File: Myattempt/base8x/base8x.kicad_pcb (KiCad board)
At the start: 4 copper layers, 350 x 110 mm, 58 parts, among them J1 Conn_02x05_Odd_Even, J10 Conn_02x14_Counter_Clockwise, J11 Conn_02x14_Counter_Clockwise, J12 Conn_02x14_Counter_Clockwise, J13 Conn_02x14_Counter_Clockwise, J14 Conn_02x14_Counter_Clockwise, J15 Conn_02x14_Counter_Clockwise, J16 Conn_01x14, J2 GS3, J3 Conn_02x14_Counter_Clockwise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

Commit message: My work implementing resistor for sensor
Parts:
- removed J10, J11, J12, J13, J14, J15: Conn_02x14_Counter_Clockwise, Connector_PinSocket_2.54mm:PinSocket_2x14_P2.54mm_Vertical
- removed J16: Conn_01x14, Connector_PinSocket_2.54mm:PinSocket_1x14_P2.54mm_Vertical
- added Raspberry_header1: Conn_02x20_Odd_Even, Connector_PinSocket_2.54mm:PinSocket_2x20_P2.54mm_Vertical, F.Cu at (-51.4, -26.7)
- added Resistor1: 4.7k, Resistor_THT:R_Axial_DIN0617_L17.0mm_D6.0mm_P20.32mm_Horizontal, F.Cu at (-94.0, -10.8)
- added Temp_sensor1: Conn_01x03_Female, Connector_PinSocket_2.54mm:PinSocket_1x03_P2.54mm_Vertical, F.Cu at (-110.5, -13.3)
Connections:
- J3 pad 10: Net-(J3-Pad10) -> SCL
- J3 pad 14: Net-(J3-Pad14) -> MISO
- J3 pad 16: Net-(J3-Pad16) -> MOSI
- J3 pad 8: Net-(J3-Pad8) -> SDA
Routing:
- net +3V3: track 37.4 -> 189.2 mm
- net GND: track 1.57 -> 77.4 mm
- net CLK0: track 0.00 -> 72.7 mm
- net +5V: track 2.43 -> 55.2 mm
- net SCL: track 139.5 -> 180.1 mm
- net SDA: track 130.8 -> 171.5 mm
- net MOSI: track 93.0 -> 129.0 mm
- net MISO: track 90.2 -> 124.2 mm

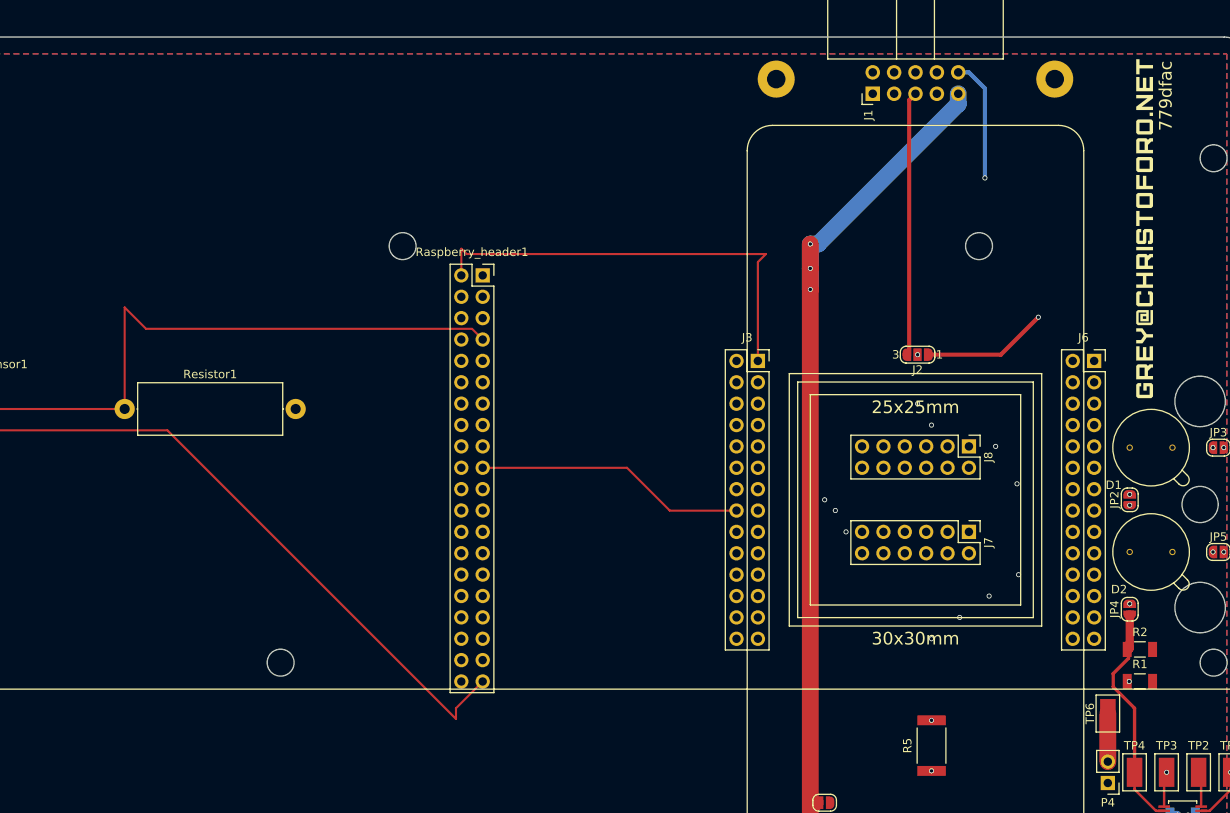
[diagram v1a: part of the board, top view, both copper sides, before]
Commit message: adding ssr and sensor
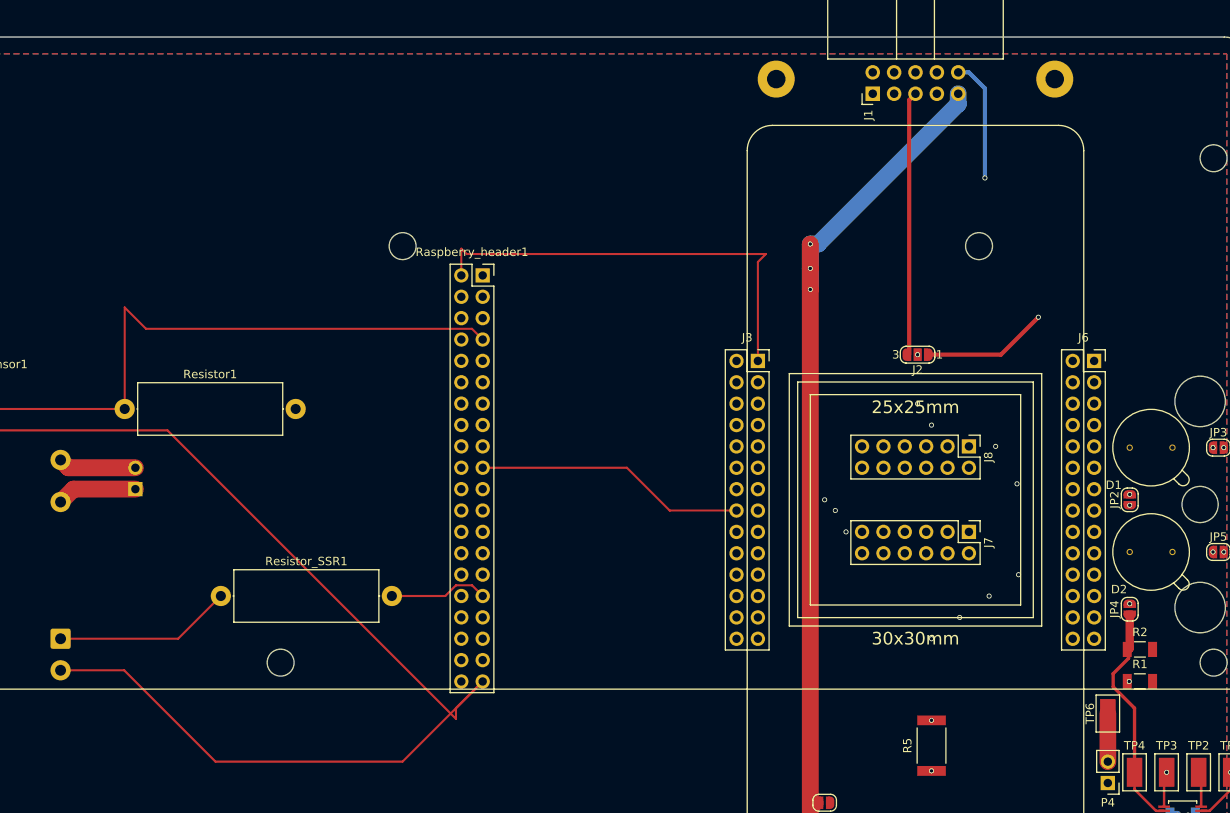
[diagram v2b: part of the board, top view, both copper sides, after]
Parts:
- removed L1: GREY@CHRISTOFORO.NET, myParts:logo
- added Resistor_SSR1: ?, Resistor_THT:R_Axial_DIN0617_L17.0mm_D6.0mm_P20.32mm_Horizontal, F.Cu at (-82.5, 11.4)
- added SSR-Ithink1: 34.81-7048, OptoDevice:Finder_34.81, B.Cu at (-101.6, 16.5)
- added SSR_connector1: Conn_01x02_Female, Connector_PinSocket_2.54mm:PinSocket_1x02_P2.54mm_Vertical, B.Cu at (-92.7, -1.27)
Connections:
- Raspberry_header1 pad 31: Net-(Raspberry_header1-Pad31) -> GPIO6
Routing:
- net GND: track 77.4 -> 136.0 mm
- net Net-(Resistor_SSR1-Pad1): track 0.00 -> 21.2 mm
- net GPIO6: track 0.00 -> 11.8 mm
- net Net-(SSR-Ithink1-Pad11): track 0.00 -> 9.52 mm
- net Net-(SSR-Ithink1-Pad14): track 0.00 -> 9.28 mm
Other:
- board text removed: "779dfac"

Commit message: SSR Changes
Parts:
- moved SSR-Ithink1 9.61 mm to (-111.1, 15.2)
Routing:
- net GND: track 136.0 -> 176.0 mm
- net Net-(Resistor_SSR1-Pad1): track 21.2 -> 52.4 mm
- net Net-(SSR-Ithink1-Pad11): track 9.52 -> 21.0 mm
- net Net-(SSR-Ithink1-Pad14): track 9.28 -> 20.8 mm
